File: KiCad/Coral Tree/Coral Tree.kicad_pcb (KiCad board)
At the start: 2 copper layers, 113.5 x 90.7 mm, 42 parts, among them J1 TRRS Connector, SW1 Key switch, SW10 Key switch, SW11 Key switch, SW12 Key switch, SW13 Key switch, SW14 Key switch, SW15 Key switch, SW16 Key switch, SW17 Key switch, SW18 Key switch, SW2 Key switch, SW3 Key switch, SW4 Key switch, SW5 Key switch, SW6 Key switch, SW7 Key switch, SW8 Key switch, SW9 Key switch, U1 nice_nano_v2

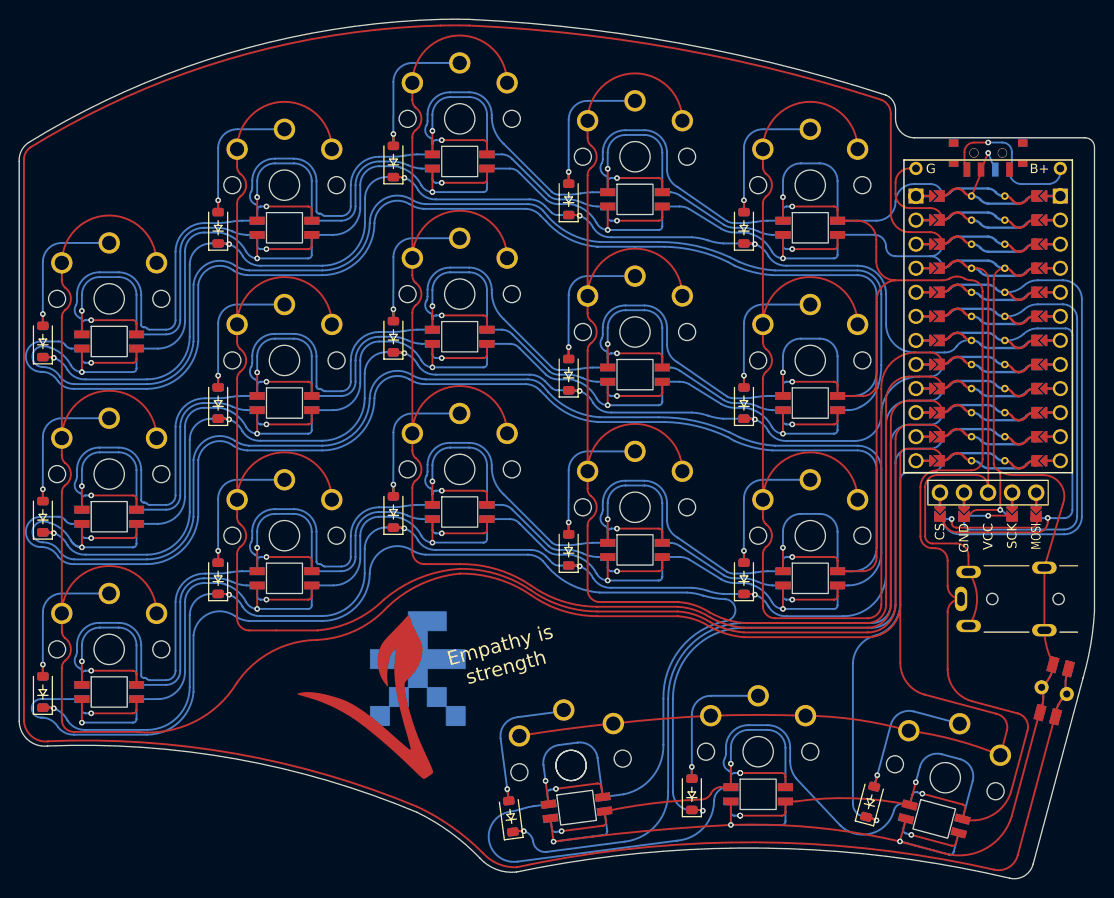
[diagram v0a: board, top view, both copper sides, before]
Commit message: Move ring col -2mm and pinky -6mm
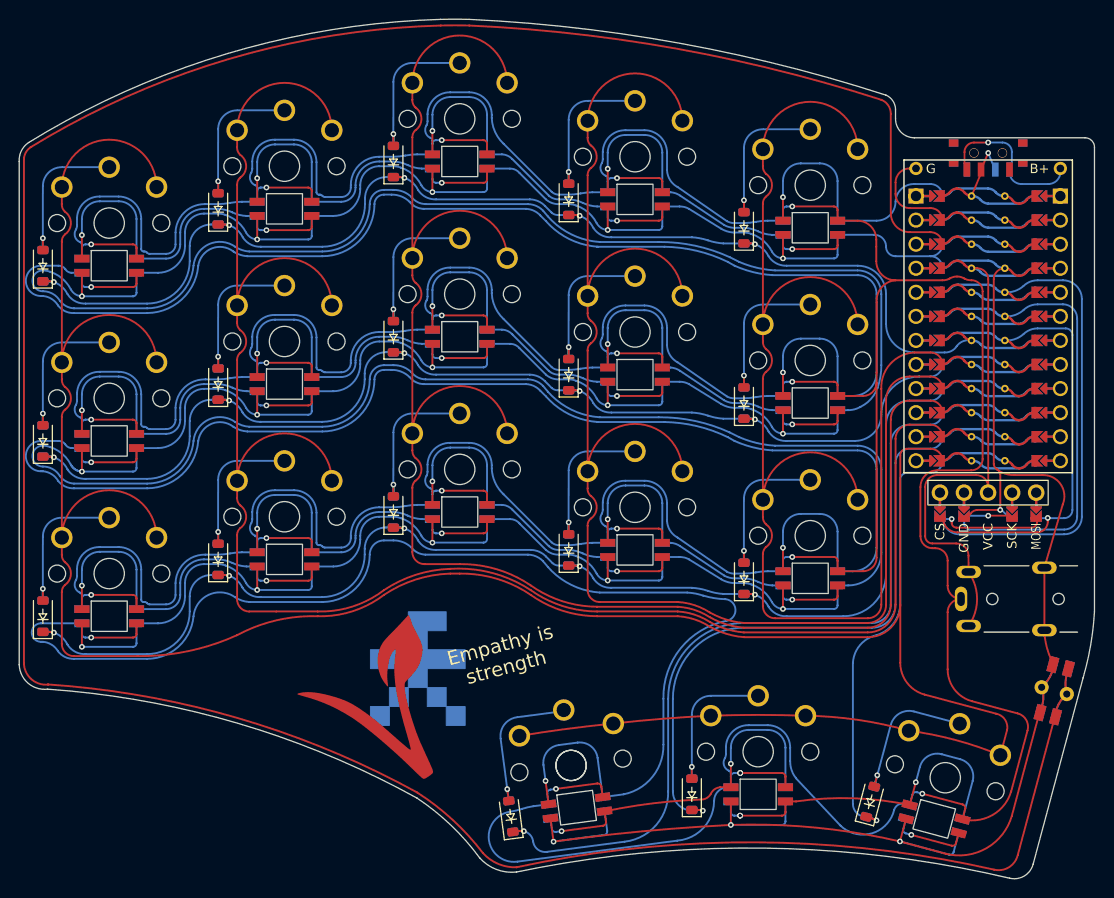
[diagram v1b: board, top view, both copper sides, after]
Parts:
- moved D10 8.00 mm to (127.0, 109.0)
- moved D15 8.00 mm to (127.0, 127.5)
- moved D5 8.00 mm to (127.0, 90.5)
- moved SW10 8.00 mm to (134.0, 104.5)
- moved SW15 8.00 mm to (134.0, 123.0)
- moved SW5 8.00 mm to (134.0, 86.0)
- moved D14 2.00 mm to (145.5, 121.5)
- moved D4 2.00 mm to (145.5, 84.5)
- moved D9 2.00 mm to (145.5, 103.0)
- moved SW14 2.00 mm to (152.5, 117.0)
- moved SW4 2.00 mm to (152.5, 80.0)
- moved SW9 2.00 mm to (152.5, 98.5)
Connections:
- Display1 pad 2: (no net) -> SCK
- J1 pad 3: unconnected-(J1-Pad3) -> 3V3
- SW10 pad 1: Net-(SW10-K) -> GND
- SW12 pad 1: Net-(SW12-K) -> GND
- SW13 pad 1: Net-(SW13-K) -> GND
- SW14 pad 1: Net-(SW14-K) -> GND
- SW15 pad 1: Net-(SW10-K) -> GND
- SW16 pad 1: Net-(SW10-K) -> GND
- SW16 pad 4: unconnected-(SW16-Dout-Pad4)_4 -> (no net)
- SW17 pad 1: Net-(SW10-K) -> GND
- SW18 pad 1: Net-(SW10-K) -> GND
- SW2 pad 1: Net-(SW12-K) -> GND
- SW3 pad 1: Net-(SW13-K) -> GND
- SW4 pad 1: Net-(SW14-K) -> GND
- SW5 pad 1: Net-(SW10-K) -> GND
- SW7 pad 1: Net-(SW12-K) -> GND
- SW8 pad 1: Net-(SW13-K) -> GND
- SW9 pad 1: Net-(SW14-K) -> GND
- SW_POWER1 pad 1: unconnected-(SW_POWER1-A-Pad1) -> (no net)
- U1 pad 19: unconnected-(U1-P0.29/D20-Pad19)_3 -> (no net)
- U1 pad 2: unconnected-(U1-D0/P0.08-RX-Pad2)_2 -> (no net)
- U1 pad 20: unconnected-(U1-P0.31/D21-Pad20)_4 -> (no net)
- U1 pad 24: RAW -> BT+
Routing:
- net Net-(D6-A): track 11.7 -> 4.92 mm
- net unconnected-(SW16-Dout-Pad4): vias 1 -> 0
- net SCK: vias 0 -> 1
- net ROW4: vias 0 -> 1
- net ROW3: vias 0 -> 1
- net ROW1: vias 4 -> 5
- net Net-(SW9-Dout): vias 1 -> 0
- net Net-(SW8-Dout): vias 3 -> 2
- net Net-(SW7-Dout): vias 4 -> 2
- net Net-(SW5-Dout): vias 1 -> 2
- net Net-(SW18-Dout): vias 3 -> 2
- net Net-(SW13-Dout): vias 1 -> 2
- net Net-(SW11-Dout): vias 2 -> 1
- net Net-(SW10-Dout): vias 2 -> 3
- net Net-(D8-A): vias 2 -> 1
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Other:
- outline, holes or cut-outs redrawn
